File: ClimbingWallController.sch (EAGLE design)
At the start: 336 parts, among them IC1 74HCT138D, IC2 74HCT138D, IC3 PIC24FJ32GB004, IC4 SN74LV4052AD, IC5 SN74LV4052AD, IC6 TC1015, IC7 NCP1117, J1 PWR, Q1 NC, Q10 DPBT8105, Q11 DPBT8105, Q12 DPBT8105, Q13 DPBT8105, Q14 DPBT8105, Q15 DPBT8105, Q16 DPBT8105, Q18 DPBT8105, Q2 DPBT8105, Q3 DPBT8105, Q4 DPBT8105, Q5 DPBT8105, Q6 DPBT8105, Q7 DPBT8105, Q8 DPBT8105, Q9 DPBT8105, X1 MINI-USB-32005-201

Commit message: Iterated through a few possible board floorplans.  Routing will be incredibly tight, but I thought of a few possibilities that ease those concerns.
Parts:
- removed Q18: DPBT8105, Parts:DPBT8105
- removed ROW0: (no value), Parts:OSTVN08A150
- removed SG1: NC, buzzer:F/CM04P
- added JP2: BUZZER, pinhead:PINHD-1X2
- added Q17: NC, transistor:-NPN-SOT23-EBC
- added ROW2: (no value), Parts:OSTVN08A150
- C1, C9: value 10uF -> 22n; device rcl:C-USC1206K -> resistor:C-USC0603
- C10, C15: value 1uF -> 22n; device rcl:C-USC0805 -> resistor:C-USC0603
- C11, C12, C13, C14, C3, C4, C5: value 0.1uF -> 22n; device rcl:C-USC0805 -> resistor:C-USC0603
- C16: value 0.1uF -> NC; device rcl:C-USC0805 -> rcl:C-USC0603K
- C17, C29: value 1uF -> 0.1uF; device rcl:C-USC0805 -> rcl:C-USC0603K
- C18, C39, C89, C90, C91, C92, C93, C94, C95, C96, C97, C98: device rcl:C-USC0805 -> rcl:C-USC0603K
- C19: value 100uF -> 0.1uF; device resistor:CPOL-USD -> rcl:C-USC0603K
- C2, C6, C7: value NC -> 22n; device rcl:C-USC0805 -> resistor:C-USC0603
- C20: device resistor:C-USC0805 -> resistor:C-USC0603
- C21: value 100uF -> NC; device resistor:CPOL-USD -> rcl:C-USC0603K
- C22: value 22n -> NC; device resistor:C-USC0805 -> rcl:C-USC0603K
- C23: value 22n -> 470pF; device resistor:C-USC0805 -> rcl:C-USC0805
- C24, C38: value 22n -> 10uF; device resistor:C-USC0805 -> rcl:C-USC1206K
- C25: value 22n -> 1uF; device resistor:C-USC0805 -> rcl:C-USC0805
- C26, C27, C28, C31, C33: value 22n -> 0.1uF; device resistor:C-USC0805 -> rcl:C-USC0603K
- C30: value 100uF -> 1uF; device resistor:CPOL-USD -> rcl:C-USC0603K
- C32, C36: value 22n -> 1uF; device resistor:C-USC0805 -> rcl:C-USC0603K
- C34, C35, C37: value 22n -> 100uF; device resistor:C-USC0805 -> resistor:CPOL-USD
- C41, C42, C43, C44, C45, C46, C47, C48, C49, C50, C51, C52, C53, C54, C55, C56, C57, C58, C59, C60, C61, C62, C63, C64, C65, C66, C67, C68, C69, C70, C71, C72, C73, C74, C75, C76, C77, C78, C79, C80, C81, C82, C83, C84, C85, C86, C87, C88: device resistor:C-USC0805 -> resistor:C-USC0603K
- C8: value 470pF -> 22n; device rcl:C-USC0805 -> resistor:C-USC0603
- Q1: value NC -> DPBT8105; device transistor:-NPN-SOT23-EBC -> Parts:DPBT8105
- R1, R10, R4: value 4.7k -> 20; device resistor:R-US_R0805 -> resistor:R-US_R0603
- R100, R101, R102, R103, R104, R105, R106, R107, R108, R109, R110, R111, R112, R113, R114, R115, R116, R117, R118, R119, R120, R121, R122, R123, R124, R125, R126, R127, R128, R129, R130, R131, R132, R133, R134, R135, R39, R40, R41, R42, R43, R44, R45, R46, R47, R48, R87, R88, R89, R90, R91, R92, R93, R94, R95, R96, R97, R98, R99: device resistor:R-US_R0805 -> resistor:R-US_R0603
- R11, R2, R5: value 4.7k -> 750; device resistor:R-US_R0805 -> resistor:R-US_R0603
- R12, R3, R6, R9: value 4.7k -> NC; device resistor:R-US_R0805 -> resistor:R-US_R0603
- R13, R16, R19, R22, R25, R28, R31, R34: value 390 -> 20; device resistor:R-US_R0805 -> resistor:R-US_R0603
- R14, R17, R20, R23, R26, R29, R32, R35: value 390 -> 750; device resistor:R-US_R0805 -> resistor:R-US_R0603
- R15, R18, R21, R24, R27, R30, R33: value 390 -> NC; device resistor:R-US_R0805 -> resistor:R-US_R0603
- R36: value 0 -> NC; device resistor:R-US_R0805 -> resistor:R-US_R0603
- R37: value NC -> 20; device resistor:R-US_R0805 -> resistor:R-US_R0603
- R38: value NC -> 750; device resistor:R-US_R0805 -> resistor:R-US_R0603
- R49, R52, R58: value 20 -> 4.7k; device resistor:R-US_R0805 -> resistor:R-US_R0603
- R50, R53, R59: value 750 -> 4.7k; device resistor:R-US_R0805 -> resistor:R-US_R0603
- R51, R54, R57, R60: value NC -> 4.7k; device resistor:R-US_R0805 -> resistor:R-US_R0603
- R55: value 20 -> 1.37k 0.5%
- R56: value 750 -> 1.37k 0.5%
- R61, R64, R67, R70, R73, R76, R79, R82: value 20 -> 390; device resistor:R-US_R0805 -> resistor:R-US_R0603
- R62, R65, R68, R71, R74, R77, R80, R83: value 750 -> 390; device resistor:R-US_R0805 -> resistor:R-US_R0603
- R63, R66, R69, R72, R75, R78, R81: value NC -> 390; device resistor:R-US_R0805 -> resistor:R-US_R0603
- R7: value 1.37k 0.5% -> 20; device resistor:R-US_R0805 -> resistor:R-US_R0603
- R8: value 1.37k 0.5% -> 750; device resistor:R-US_R0805 -> resistor:R-US_R0603
- R84: value NC -> 0
- R85: value 20 -> NC; device resistor:R-US_R0805 -> resistor:R-US_R0603
- R86: value 750 -> NC; device resistor:R-US_R0805 -> resistor:R-US_R0603
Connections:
- removed net N$31: Q1.B, R39.2
- removed net N$32: Q1.C, SG1.2
- removed net N$35: Q3.B, R44.2, R45.2
- removed net N$36: C22.1, R43.1
- removed net N$37: Q4.B, R47.2, R48.2
- removed net N$38: C23.1, R46.1
- removed net N$39: Q5.B, R50.2, R51.2
- removed net N$40: C24.1, R49.1
- removed net N$49: Q18.B, R65.2, R66.2
- removed net N$50: C31.1, R64.1
- removed net N$51: Q10.B, R68.2, R69.2
- removed net N$52: C32.1, R67.1
- removed net N$53: Q11.B, R71.2, R72.2
- removed net N$54: C33.1, R70.1
- removed net N$55: Q12.B, R74.2, R75.2
- removed net N$56: C34.1, R73.1
- removed net N$57: Q13.B, R77.2, R78.2
- removed net N$58: C35.1, R76.1
- removed net N$59: Q14.B, R80.2, R81.2
- removed net N$60: C36.1, R79.1
- removed net N$61: Q15.B, R83.2, R84.2
- removed net N$62: C37.1, R82.1
- removed net N$63: Q16.B, R86.2, R87.2
- removed net N$64: C38.1, R85.1
- new net N$65: R64.2, TCH0-3.KL
- new net N$66: R65.2, TCH0-4.KL
- new net N$67: R66.2, TCH0-5.KL
- new net N$68: R67.2, TCH0-6.KL
- new net N$69: R68.2, TCH0-7.KL
- new net N$70: R69.2, TCH0-8.KL
- new net N$71: R70.2, TCH0-9.KL
- new net N$72: R71.2, TCH0-10.KL
- new net N$73: R72.2, TCH0-11.KL
- new net N$74: R74.2, TCH1-2.KL
- new net N$75: R76.2, TCH1-4.KL
- new net N$76: R78.2, TCH1-6.KL
- new net N$77: R80.2, TCH1-8.KL
- new net N$78: R82.2, TCH1-10.KL
- new net N$79: R73.2, TCH1-1.KL
- new net N$80: R75.2, TCH1-3.KL
- new net N$81: R77.2, TCH1-5.KL
- new net N$82: R79.2, TCH1-7.KL
- new net N$83: R81.2, TCH1-9.KL
- new net N$84: R83.2, TCH1-11.KL
- new net N$85: C23.1, IC6.BYPASS
- new net N$86: R85.1, R86.2
- new net N$87: Q17.B, R87.2
- new net N$88: JP2.2, Q17.C
- net +3V3: now also C19.1, C24.1, C26.1, C27.1, C30.1, C31.1, C32.1, C33.1, R60.2, R85.2; no longer C11.1, C12.1, C15.1, C16.1, C3.1, C4.1, C5.1, C9.1, R12.2, R37.2
- net +5V: now also C25.1, C28.1, C34.+, C36.1, C37.+, JP2.1, Q1.E, R12.1, R15.1, R18.1, R21.1, R24.1, R27.1, R3.1, R30.1, R33.1, R36.1, R39.1, R6.1, R84.2, R9.1; no longer C10.1, C13.1, C14.1, C21.+, C30.+, Q18.E, R36.2, R51.1, R54.1, R57.1, R60.1, R63.1, R66.1, R69.1, R72.1, R75.1, R78.1, R81.1, R84.1, R87.1, SG1.1
- net CAIREF: now also R55.2; no longer R7.2
- net CAIREF1: now also R56.2; no longer R8.2
- net DISVREG: now also R59.2; no longer R11.2
- net GND: now also C19.2, C21.2, C30.2, C34.-, C35.-, C37.-, Q17.E, R49.1, R50.1, R51.1, R52.1, R53.1, R54.1, R55.1, R56.1, R57.1, R59.1, R86.1; no longer C19.-, C21.-, C30.-, C34.2, C35.2, C37.2, Q1.E, R1.1, R11.1, R2.1, R3.1, R38.1, R4.1, R5.1, R6.1, R7.1, R8.1, R9.1
- net MCLR_: now also R61.1; no longer R13.1
- net N$1: now also Q1.B, R2.2, R3.2; no longer C2.1, R12.1, R13.2
- net N$10: now also C5.1, R13.1; no longer R17.2, TCH0-4.KL
- net N$11: now also Q7.B, R17.2; no longer TCH0-5.KL
- net N$12: now also C6.1, R16.1; no longer R19.2, TCH0-6.KL
- net N$13: now also Q8.B, R21.2; no longer TCH0-7.KL
- net N$14: now also C7.1, R19.1; no longer R21.2, TCH0-8.KL
- net N$15: now also Q9.B, R23.2, R24.2; no longer R22.2, TCH0-9.KL
- net N$16: now also C8.1, R22.1; no longer R23.2, TCH0-10.KL
- net N$17: now also Q10.B, R26.2, R27.2; no longer R24.2, TCH0-11.KL
- net N$18: now also C9.1, R25.1; no longer R26.2, TCH1-2.KL
- net N$19: now also Q11.B, R29.2, R30.2; no longer R28.2, TCH1-4.KL
- net N$2: now also C1.1, R1.1; no longer IC1.G2A, IC1.G2B, R2.2
- net N$20: now also C10.1, R28.1; no longer R30.2, TCH1-6.KL
- net N$21: now also Q12.B, R33.2; no longer TCH1-8.KL
- net N$22: now also C11.1, R31.1; no longer R34.2, TCH1-10.KL
- net N$23: now also Q13.B, R35.2, R36.2; no longer R25.2, TCH1-1.KL
- net N$24: now also C12.1, R34.1; no longer R27.2, TCH1-3.KL
- net N$25: now also Q14.B, R38.2, R39.2; no longer R29.2, TCH1-5.KL
- net N$26: now also C13.1, R37.1; no longer R31.2, TCH1-7.KL
- net N$27: now also Q15.B, R44.2, R45.2; no longer R33.2, TCH1-9.KL
- net N$28: now also C14.1, R43.1; no longer R35.2, TCH1-11.KL
- net N$29: now also Q16.B, R47.2, R48.2; no longer C8.1, IC6.BYPASS
- net N$3: now also Q3.B, R5.2, R6.2; no longer IC4.INH, R3.2
- net N$30: now also C15.1, R46.1; no longer R37.1, R38.2
- net N$4: now also C2.1, R4.1; no longer IC3.VBUS, R10.2
- net N$41: now also IC1.G2A, IC1.G2B, R50.2; no longer Q6.B, R53.2, R54.2
- net N$42: now also IC4.INH, R51.2; no longer C25.1, R52.1
- net N$43: now also IC2.G2A, IC2.G2B, R53.2; no longer Q7.B, R56.2, R57.2
- net N$44: now also IC5.INH, R54.2; no longer C26.1, R55.1
- net N$45: now also IC3.VBUS, R58.2; no longer Q8.B, R59.2, R60.2
- net N$46: now also C16.1, R60.1, R61.2; no longer C27.1, R58.1
- net N$47: now also TCH0-1.KL; no longer Q9.B, R63.2
- net N$48: now also R63.2, TCH0-2.KL; no longer C28.1, R61.1
- net N$5: now also Q4.B, R8.2, R9.2; no longer IC2.G2A, IC2.G2B, R5.2
- net N$6: now also C3.1, R7.1; no longer IC5.INH, R6.2
- net N$7: now also Q5.B, R11.2, R12.2; no longer R14.2, TCH0-1.KL
- net N$8: now also C4.1, R10.1; no longer R15.2, TCH0-2.KL
- net N$9: now also Q6.B, R14.2, R15.2; no longer R16.2, TCH0-3.KL
- net OSCI: now also C22.1; no longer C7.1
- net OSCO: now also C21.1; no longer C6.1
- net RAEN: now also R49.2; no longer R1.2
- net RBEN: now also R52.2; no longer R4.2
- net ROW0: now also Q1.C, R1.2, ROW1-1.KL; no longer Q2.C, R40.2, ROW0-1.KL
- net ROW0EN_: now also R2.1; no longer R41.1
- net ROW1: now also Q2.C, R40.2, ROW1-2.KL; no longer Q3.C, R43.2, ROW0-2.KL
- net ROW10: now also D12.C, Q12.C, R31.2, ROW2-4.KL; no longer D11.C, Q11.C, R70.2, ROW1-3.KL
- net ROW10EN_: now also R32.1; no longer R71.1
- net ROW11: now also D14.C, Q14.C, R37.2, ROW2-5.KL; no longer D12.C, Q12.C, R73.2, ROW1-4.KL
- net ROW11EN_: now also R38.1; no longer R74.1
- net ROW12: now also D15.C, Q15.C, R43.2, ROW2-7.KL; no longer D13.C, Q13.C, R76.2, ROW1-5.KL
- net ROW12EN_: now also R44.1; no longer R77.1
- net ROW13: now also D16.C, Q16.C, R46.2, ROW2-8.KL; no longer D14.C, Q14.C, R79.2, ROW1-6.KL
- net ROW13EN_: now also R47.1; no longer R80.1
- net ROW14: now also D9.C, Q9.C, R22.2, ROW2-2.KL; no longer D15.C, Q15.C, R82.2, ROW1-7.KL
- net ROW14EN_: now also R23.1; no longer R83.1
- net ROW15: now also D13.C, Q13.C, R34.2, ROW2-6.KL; no longer D16.C, Q16.C, R85.2, ROW1-8.KL
- net ROW15EN_: now also R35.1; no longer R86.1
- net ROW1EN_: now also R41.1; no longer R44.1
- net ROW2: now also Q3.C, R4.2, ROW1-3.KL; no longer Q4.C, R46.2, ROW0-3.KL
- net ROW2EN_: now also R5.1; no longer R47.1
- net ROW3: now also Q4.C, R7.2, ROW1-4.KL; no longer Q5.C, R49.2, ROW0-4.KL
- net ROW3EN_: now also R8.1; no longer R50.1
- net ROW4: now also D6.C, R13.2, ROW1-5.KL; no longer D5.C, R52.2, ROW0-5.KL
- net ROW4EN_: now also R14.1; no longer R53.1
- net ROW5: now also D5.C, Q5.C, R10.2, ROW1-6.KL; no longer D6.C, Q7.C, R55.2, ROW0-6.KL
- net ROW5EN_: now also R11.1; no longer R56.1
- net ROW6: now also Q7.C, R16.2, ROW1-7.KL; no longer Q8.C, R58.2, ROW0-7.KL
- net ROW6EN_: now also R17.1; no longer R59.1
- net ROW7: now also Q8.C, R19.2, ROW1-8.KL; no longer Q9.C, R61.2, ROW0-8.KL
- net ROW7EN_: now also R20.1; no longer R62.1
- net ROW8: now also D10.C, Q10.C, R25.2, ROW2-1.KL; no longer D9.C, Q18.C, R64.2, ROW1-1.KL
- net ROW8EN_: now also R26.1; no longer R65.1
- net ROW9: now also D11.C, Q11.C, R28.2, ROW2-3.KL; no longer D10.C, Q10.C, R67.2, ROW1-2.KL
- net ROW9EN_: now also R29.1; no longer R68.1
- net TOUCH0: now also R62.1; no longer R14.1
- net TOUCH1: now also R63.1; no longer R15.1
- net TOUCH10: now also R72.1; no longer R24.1
- net TOUCH11: now also R73.1; no longer R25.1
- net TOUCH12: now also R74.1; no longer R26.1
- net TOUCH13: now also R75.1; no longer R27.1
- net TOUCH14: now also R76.1; no longer R28.1
- net TOUCH15: now also R77.1; no longer R29.1
- net TOUCH16: now also R78.1; no longer R30.1
- net TOUCH17: now also R79.1; no longer R31.1
- net TOUCH18: now also R80.1; no longer R32.1
- net TOUCH19: now also R81.1; no longer R33.1
- net TOUCH2: now also R64.1; no longer R16.1
- net TOUCH20: now also R82.1; no longer R34.1
- net TOUCH21: now also R83.1; no longer R35.1
- net TOUCH3: now also R65.1; no longer R17.1
- net TOUCH4: now also R66.1; no longer R18.1
- net TOUCH5: now also R67.1; no longer R19.1
- net TOUCH6: now also R68.1; no longer R20.1
- net TOUCH7: now also R69.1; no longer R21.1
- net TOUCH8: now also R70.1; no longer R22.1
- net TOUCH9: now also R71.1; no longer R23.1
- net V+: now also C35.+, R84.1; no longer C19.+, R36.1
- net VBUS: now also R57.2, R58.1; no longer R10.1, R9.2
- net VDDCORE: now also C38.1; no longer C1.1
- net VREF+: now also R87.1; no longer R39.1
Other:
- moved on the sheet: C1, C10, C11, C12, C13, C14, C15, C16, C17, C18, C2, C20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

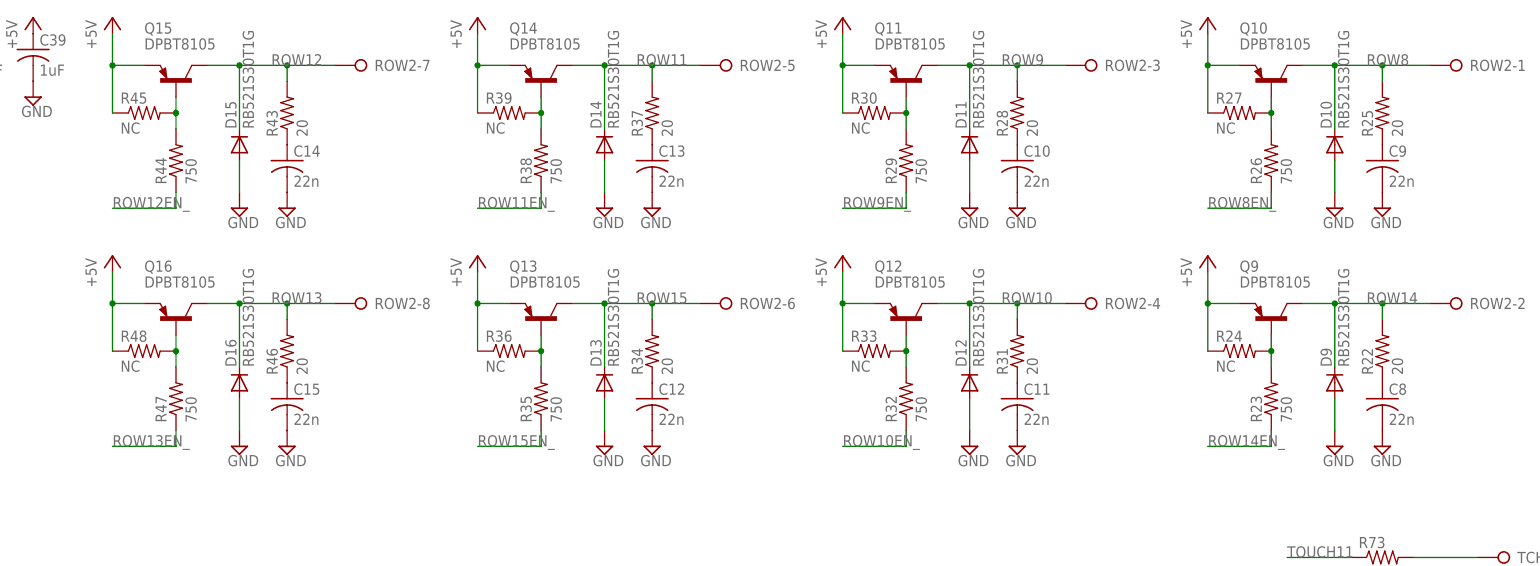
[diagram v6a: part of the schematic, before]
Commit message: Completed most of the column driver routing.
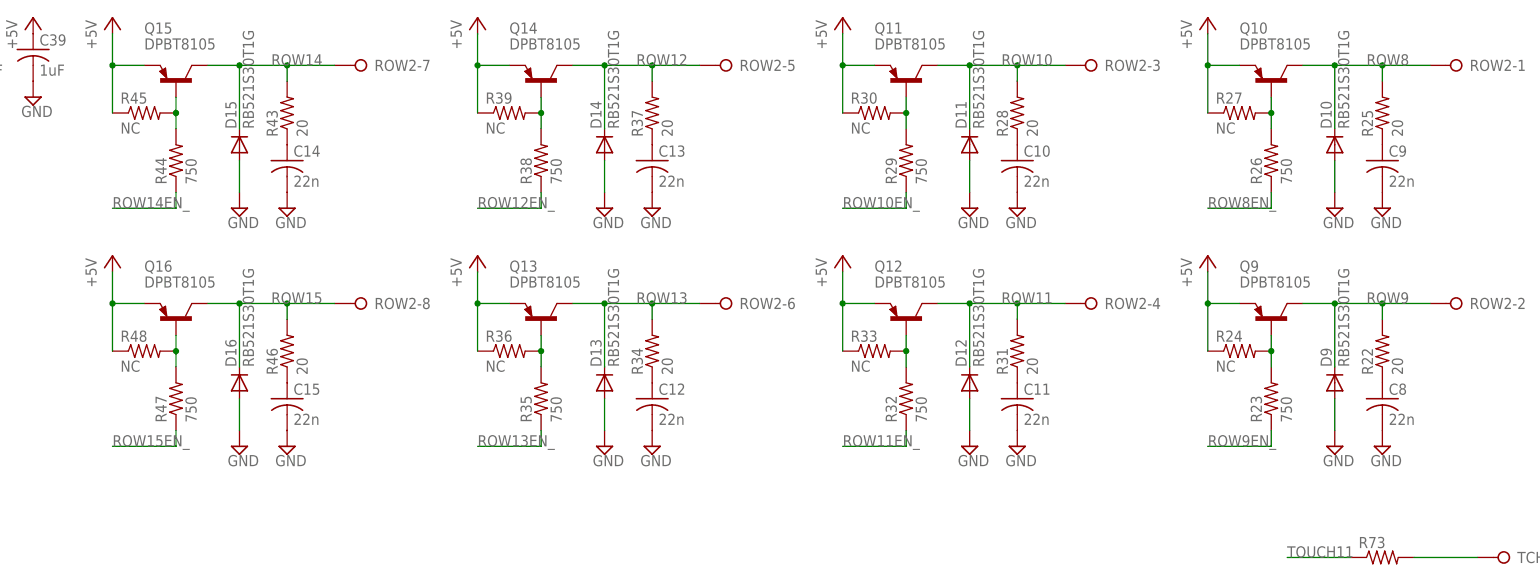
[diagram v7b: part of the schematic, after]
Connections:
- net ROW10: now also D11.C, Q11.C, R28.2, ROW2-3.KL; no longer D12.C, Q12.C, R31.2, ROW2-4.KL
- net ROW10EN_: now also R29.1; no longer R32.1
- net ROW11: now also D12.C, Q12.C, R31.2, ROW2-4.KL; no longer D14.C, Q14.C, R37.2, ROW2-5.KL
- net ROW11EN_: now also R32.1; no longer R38.1
- net ROW12: now also D14.C, Q14.C, R37.2, ROW2-5.KL; no longer D15.C, Q15.C, R43.2, ROW2-7.KL
- net ROW12EN_: now also R38.1; no longer R44.1
- net ROW13: now also D13.C, Q13.C, R34.2, ROW2-6.KL; no longer D16.C, Q16.C, R46.2, ROW2-8.KL
- net ROW13EN_: now also R35.1; no longer R47.1
- net ROW14: now also D15.C, Q15.C, R43.2, ROW2-7.KL; no longer D9.C, Q9.C, R22.2, ROW2-2.KL
- net ROW14EN_: now also R44.1; no longer R23.1
- net ROW15: now also D16.C, Q16.C, R46.2, ROW2-8.KL; no longer D13.C, Q13.C, R34.2, ROW2-6.KL
- net ROW15EN_: now also R47.1; no longer R35.1
- net ROW9: now also D9.C, Q9.C, R22.2, ROW2-2.KL; no longer D11.C, Q11.C, R28.2, ROW2-3.KL
- net ROW9EN_: now also R23.1; no longer R29.1

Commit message: Made progress on layout.
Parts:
- C23, C25: device rcl:C-USC0805 -> rcl:C-USC0603K
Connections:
- net TOUCH0: now also IC3.AN4; no longer IC4.Y0
- net TOUCH1: now also IC3.AN1; no longer IC4.Y1
- net TOUCH10: now also IC4.X3; no longer IC3.AN4
- net TOUCH2: now also IC3.AN9; no longer IC4.Y2
- net TOUCH3: now also IC4.Y2; no longer IC4.Y3
- net TOUCH4: now also IC4.Y0; no longer IC4.X0
- net TOUCH5: now also IC4.Y3; no longer IC4.X1
- net TOUCH6: now also IC4.Y1; no longer IC4.X2
- net TOUCH7: now also IC4.X2; no longer IC4.X3
- net TOUCH8: now also IC4.X1; no longer IC3.AN9
- net TOUCH9: now also IC4.X0; no longer IC3.AN1
